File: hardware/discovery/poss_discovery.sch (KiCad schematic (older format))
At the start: 27 parts, among them SW1 SW_PUSH, SW10 SW_PUSH, SW11 SW_PUSH, SW12 SW_PUSH, SW13 SW_PUSH, SW14 SW_PUSH, SW15 SW_PUSH, SW16 SW_PUSH, SW18 SW_PUSH, SW19 SW_PUSH, SW2 SW_PUSH, SW20 SW_PUSH, SW21 SW_PUSH, SW22 SW_PUSH, SW3 SW_PUSH, SW4 SW_PUSH, SW5 SW_PUSH, SW6 SW_PUSH, SW7 SW_PUSH, SW8 SW_PUSH, SW9 SW_PUSH, U1 STM32F4_DISCO_Header, U6 encoder_and_switch, U7 encoder_and_switch

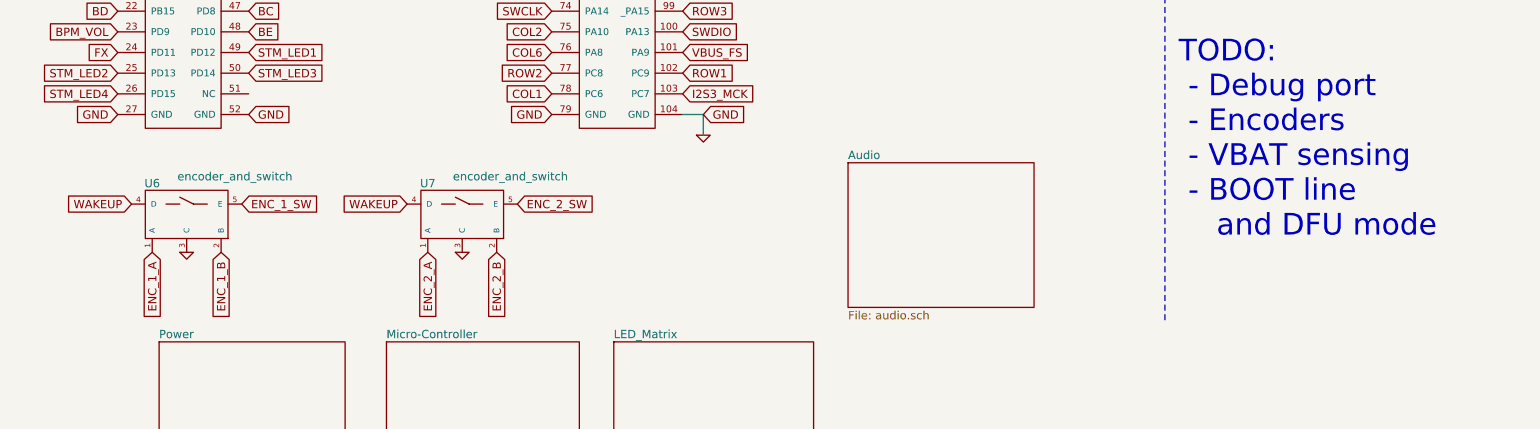
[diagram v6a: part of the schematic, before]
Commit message: Discovery: Add encoders noise filtering
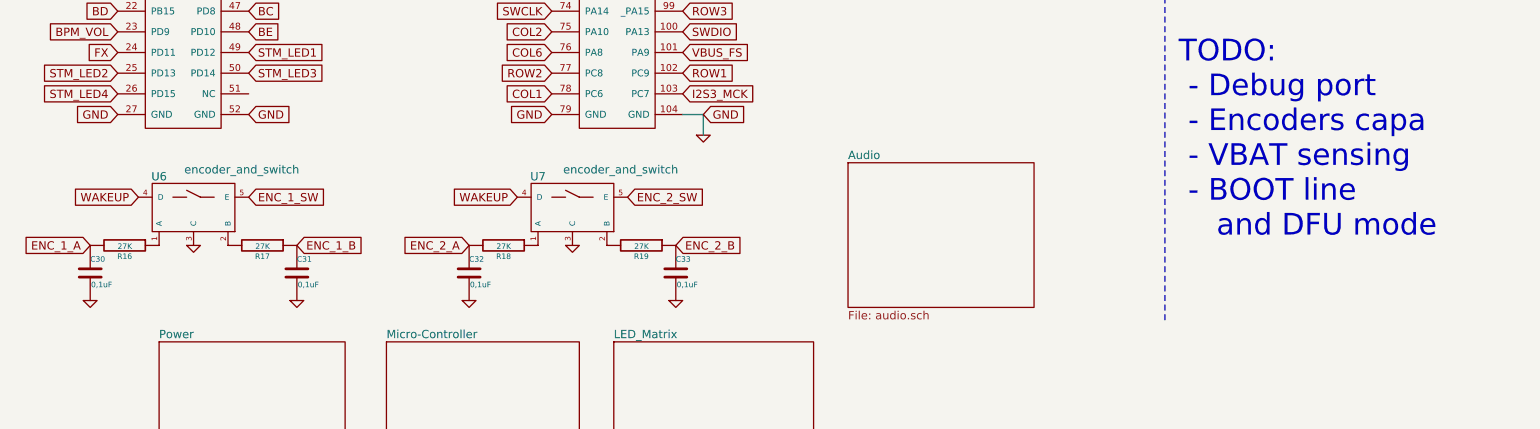
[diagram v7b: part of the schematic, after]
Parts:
- added C30, C31, C32, C33: 0,1uF, Capacitors_SMD:C_0805, symbol C
- added R16, R17, R18, R19: 27K, Resistors_SMD:R_0805, symbol R
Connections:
- net ENC_1_A: now also C30.1, R16.2; no longer U6.1 (A)
- net ENC_1_B: now also C31.1, R17.1; no longer U6.2 (B)
- net ENC_2_A: now also C32.1, R18.2; no longer U7.1 (A)
- net ENC_2_B: now also C33.1, R19.1; no longer U7.2 (B)
- net GND: now also C30.2, C31.2, C32.2, C33.2
- new net: R16.1, U6.1 (A)
- new net: R17.2, U6.2 (B)
- new net: R18.1, U7.1 (A)
- new net: R19.2, U7.2 (B)
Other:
- note added: "TODO:\n - Debug port\n - Encoders capa\n - VBAT sensing\n - BOOT line \n and DFU mode"
- note removed: "TODO:\n - Debug port\n - Encoders\n - VBAT sensing\n - BOOT line \n and DFU mode"
- moved on the sheet: U6, U7
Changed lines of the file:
@@
 GND
 $Comp
-L GND #PWR01
+L GND #PWR7
 U 1 1 585DBA46
 P 5500 5100
-F 0 "#PWR01" H 5500 5100 30  0001 C CNN
+F 0 "#PWR7" H 5500 5100 30  0001 C CNN
 F 1 "GND" H 5500 5030 30  0001 C CNN
 F 2 "" H 5500 5100 60  0001 C CNN
@@
 $EndSheet
 Text Notes 8950 5850 0    157  ~ 0
-TODO:\n - Debug port\n - Encoders\n - VBAT sensing\n - BOOT line \n    and DFU mode
+TODO:\n - Debug port\n - Encoders capa\n - VBAT sensing\n - BOOT line \n    and DFU mode
 Text GLabel 6800 3750 0    60   Input ~ 0
 WAKEUP
@@
 L encoder_and_switch U6
 U 1 1 585F9C7A
-P 1750 5250
-F 0 "U6" H 1500 5050 60  0000 C CNN
-F 1 "encoder_and_switch" H 2100 5100 60  0000 C CNN
-F 2 "stm32f4-disco:encoder_EC12D" H 1750 5250 60  0001 C CNN
-F 3 "" H 1750 5250 60  0001 C CNN
-	1    1750 5250
+P 1800 5200
+F 0 "U6" H 1550 5000 60  0000 C CNN
+F 1 "encoder_and_switch" H 2150 5050 60  0000 C CNN
+F 2 "stm32f4-disco:encoder_EC12D" H 1800 5200 60  0001 C CNN
+F 3 "" H 1800 5200 60  0001 C CNN
+	1    1800 5200
 	1    0    0    -1
 $EndComp
@@
 L encoder_and_switch U7
 U 1 1 585FA833
-P 3750 5250
-F 0 "U7" H 3500 5050 60  0000 C CNN
-F 1 "encoder_and_switch" H 4100 5100 60  0000 C CNN
-F 2 "stm32f4-disco:encoder_EC12D" H 3750 5250 60  0001 C CNN
-F 3 "" H 3750 5250 60  0001 C CNN
-	1    3750 5250
-	1    0    0    -1
-$EndComp
-Text GLabel 1350 5600 0    60   Input ~ 0
+P 4550 5200
+F 0 "U7" H 4300 5000 60  0000 C CNN
+F 1 "encoder_and_switch" H 4900 5050 60  0000 C CNN
+F 2 "stm32f4-disco:encoder_EC12D" H 4550 5200 60  0001 C CNN
+F 3 "" H 4550 5200 60  0001 C CNN
+	1    4550 5200
+	1    0    0    -1
+$EndComp
+Text GLabel 1400 5550 0    60   Input ~ 0
 WAKEUP
-Text GLabel 3350 5600 0    60   Input ~ 0
+Text GLabel 4150 5550 0    60   Input ~ 0
 WAKEUP
-Text GLabel 2150 5600 2    60   Input ~ 0
+Text GLabel 2200 5550 2    60   Input ~ 0
 ENC_1_SW
-Text GLabel 4150 5600 2    60   Input ~ 0
+Text GLabel 4950 5550 2    60   Input ~ 0
 ENC_2_SW
-Text GLabel 1500 5950 3    60   Input ~ 0
+Text GLabel 1050 5900 0    60   Input ~ 0
 ENC_1_A
-Text GLabel 2000 5950 3    60   Input ~ 0
+Text GLabel 2550 5900 2    60   Input ~ 0
 ENC_1_B
-Text GLabel 3500 5950 3    60   Input ~ 0
-ENC_2_A
-Text GLabel 4000 5950 3    60   Input ~ 0
-ENC_2_B
-$Comp
-L GND #PWR02
+$Comp
+L GND #PWR5
 U 1 1 586532D8
-P 3750 5950
-F 0 "#PWR02" H 3750 5950 30  0001 C CNN
-F 1 "GND" H 3750 5880 30  0001 C CNN
-F 2 "" H 3750 5950 60  0001 C CNN
-F 3 "" H 3750 5950 60  0001 C CNN
-	1    3750 5950
-	1    0    0    -1
-$EndComp
-$Comp
-L GND #PWR03
+P 4550 5900
+F 0 "#PWR5" H 4550 5900 30  0001 C CNN
+F 1 "GND" H 4550 5830 30  0001 C CNN
+F 2 "" H 4550 5900 60  0001 C CNN
+F 3 "" H 4550 5900 60  0001 C CNN
+	1    4550 5900
+	1    0    0    -1
+$EndComp
+$Comp
+L GND #PWR2
 U 1 1 58653337
-P 1750 5950
-F 0 "#PWR03" H 1750 5950 30  0001 C CNN
-F 1 "GND" H 1750 5880 30  0001 C CNN
-F 2 "" H 1750 5950 60  0001 C CNN
-F 3 "" H 1750 5950 60  0001 C CNN
-	1    1750 5950
+P 1800 5900
+F 0 "#PWR2" H 1800 5900 30  0001 C CNN
+F 1 "GND" H 1800 5830 30  0001 C CNN
+F 2 "" H 1800 5900 60  0001 C CNN
+F 3 "" H 1800 5900 60  0001 C CNN
+	1    1800 5900
 	1    0    0    -1
 $EndComp
@@
 Wire Wire Line
 	9950 1800 9950 3750
+$Comp
+L R R16
+U 1 1 58664AEC
+P 1300 5900
+F 0 "R16" V 1380 5900 40  0000 C CNN
+F 1 "27K" V 1307 5901 40  0000 C CNN
+F 2 "Resistors_SMD:R_0805" V 1230 5900 30  0001 C CNN
+F 3 "" H 1300 5900 30  0000 C CNN
+	1    1300 5900
+	0    1    1    0
+$EndComp
+$Comp
+L C C30
+U 1 1 58664DFD
+P 1050 6100
+F 0 "C30" H 1050 6200 40  0000 L CNN
+F 1 "0,1uF" H 1056 6015 40  0000 L CNN
+F 2 "Capacitors_SMD:C_0805" H 1088 5950 30  0001 C CNN
+F 3 "" H 1050 6100 60  0000 C CNN
+	1    1050 6100
+	1    0    0    -1
+$EndComp
+$Comp
+L GND #PWR1
+U 1 1 58664E6F
+P 1050 6300
+F 0 "#PWR1" H 1050 6300 30  0001 C CNN
+F 1 "GND" H 1050 6230 30  0001 C CNN
+F 2 "" H 1050 6300 60  0001 C CNN
+F 3 "" H 1050 6300 60  0001 C CNN
+	1    1050 6300
+	1    0    0    -1
+$EndComp
+$Comp
+L R R17
+U 1 1 586652D6
+P 2300 5900
+F 0 "R17" V 2380 5900 40  0000 C CNN
+F 1 "27K" V 2307 5901 40  0000 C CNN
+F 2 "Resistors_SMD:R_0805" V 2230 5900 30  0001 C CNN
+F 3 "" H 2300 5900 30  0000 C CNN
+	1    2300 5900
+	0    1    1    0
+$EndComp
+$Comp
+L C C31
+U 1 1 586655E8
+P 2550 6100
+F 0 "C31" H 2550 6200 40  0000 L CNN
+F 1 "0,1uF" H 2556 6015 40  0000 L CNN
+F 2 "Capacitors_SMD:C_0805" H 2588 5950 30  0001 C CNN
+F 3 "" H 2550 6100 60  0000 C CNN
+	1    2550 6100
+	1    0    0    -1
+$EndComp
+$Comp
+L GND #PWR3
+U 1 1 5866566D
+P 2550 6300
+F 0 "#PWR3" H 2550 6300 30  0001 C CNN
+F 1 "GND" H 2550 6230 30  0001 C CNN
+F 2 "" H 2550 6300 60  0001 C CNN
+F 3 "" H 2550 6300 60  0001 C CNN
+	1    2550 6300
+	1    0    0    -1
+$EndComp
+Text GLabel 5300 5900 2    60   Input ~ 0
+ENC_2_B
+$Comp
+L R R19
+U 1 1 58665F22
+P 5050 5900
+F 0 "R19" V 5130 5900 40  0000 C CNN
+F 1 "27K" V 5057 5901 40  0000 C CNN
+F 2 "Resistors_SMD:R_0805" V 4980 5900 30  0001 C CNN
+F 3 "" H 5050 5900 30  0000 C CNN
+	1    5050 5900
+	0    1    1    0
+$EndComp
+$Comp
+L C C33
+U 1 1 58665F28
+P 5300 6100
+F 0 "C33" H 5300 6200 40  0000 L CNN
+F 1 "0,1uF" H 5306 6015 40  0000 L CNN
+F 2 "Capacitors_SMD:C_0805" H 5338 5950 30  0001 C CNN
+F 3 "" H 5300 6100 60  0000 C CNN
+	1    5300 6100
+	1    0    0    -1
+$EndComp
+$Comp
+L GND #PWR6
+U 1 1 58665F2E
+P 5300 6300
+F 0 "#PWR6" H 5300 6300 30  0001 C CNN
+F 1 "GND" H 5300 6230 30  0001 C CNN
+F 2 "" H 5300 6300 60  0001 C CNN
+F 3 "" H 5300 6300 60  0001 C CNN
+	1    5300 6300
+	1    0    0    -1
+$EndComp
+Text GLabel 3800 5900 0    60   Input ~ 0
+ENC_2_A
+$Comp
+L R R18
+U 1 1 58666537
+P 4050 5900
+F 0 "R18" V 4130 5900 40  0000 C CNN
+F 1 "27K" V 4057 5901 40  0000 C CNN
+F 2 "Resistors_SMD:R_0805" V 3980 5900 30  0001 C CNN
+F 3 "" H 4050 5900 30  0000 C CNN
+	1    4050 5900
+	0    1    1    0
+$EndComp
+$Comp
+L C C32
+U 1 1 5866653D
+P 3800 6100
+F 0 "C32" H 3800 6200 40  0000 L CNN
+F 1 "0,1uF" H 3806 6015 40  0000 L CNN
+F 2 "Capacitors_SMD:C_0805" H 3838 5950 30  0001 C CNN
+F 3 "" H 3800 6100 60  0000 C CNN
+	1    3800 6100
+	1    0    0    -1
+$EndComp
+$Comp
+L GND #PWR4
+U 1 1 58666543
+P 3800 6300
+F 0 "#PWR4" H 3800 6300 30  0001 C CNN
+F 1 "GND" H 3800 6230 30  0001 C CNN
+F 2 "" H 3800 6300 60  0001 C CNN
+F 3 "" H 3800 6300 60  0001 C CNN
+	1    3800 6300
+	1    0    0    -1
+$EndComp
 $EndSCHEMATC
